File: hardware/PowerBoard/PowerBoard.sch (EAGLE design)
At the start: 134 parts, among them J1 CON-HRS-DM3AT, J2 CON-ZX62R-B-5P, J3 CON-FTSH-105-01-L-DV-K, J4 CON-S2B-PH-SM4-TB, J5 CON-PJ-102A, J6 CON-71741-0002-TOP, M1 MOUNT-HOLE3.3, M2 MOUNT-HOLE3.3, M3 MOUNT-HOLE3.3, M4 MOUNT-HOLE3.3, M5 FIDUCIAL1X2, M6 FIDUCIAL1X2, M7 FIDUCIAL1X2, M8 FIDUCIAL1X2, Q1 SI2323CDS, Q2 SI2312CDS, Q3 SI2333CDS, Q4 SI2333CDS, SW1 SWITCH-SPST, SW2 SWITCH-MS12ASG30, SW3 SWITCH-KSC-201J, U1 LTC4361-2DC, U10 MAX9938FEUK, U11 MAX9938FEUK, U12 MAX9938FEUK, U13 STM32F10XCXT6, U14 LTC2942-1, U15 USBLC6-2, U2 LTC4085, U3 XC6220B331MR-G, U4 XC6220B331MR-G, U5 XC9236A15DMR-G, U6 MIC94043, U8 MAX9938FEUK, U9 MAX9938FEUK, X1 ECX-2236, X2 ECX-31B

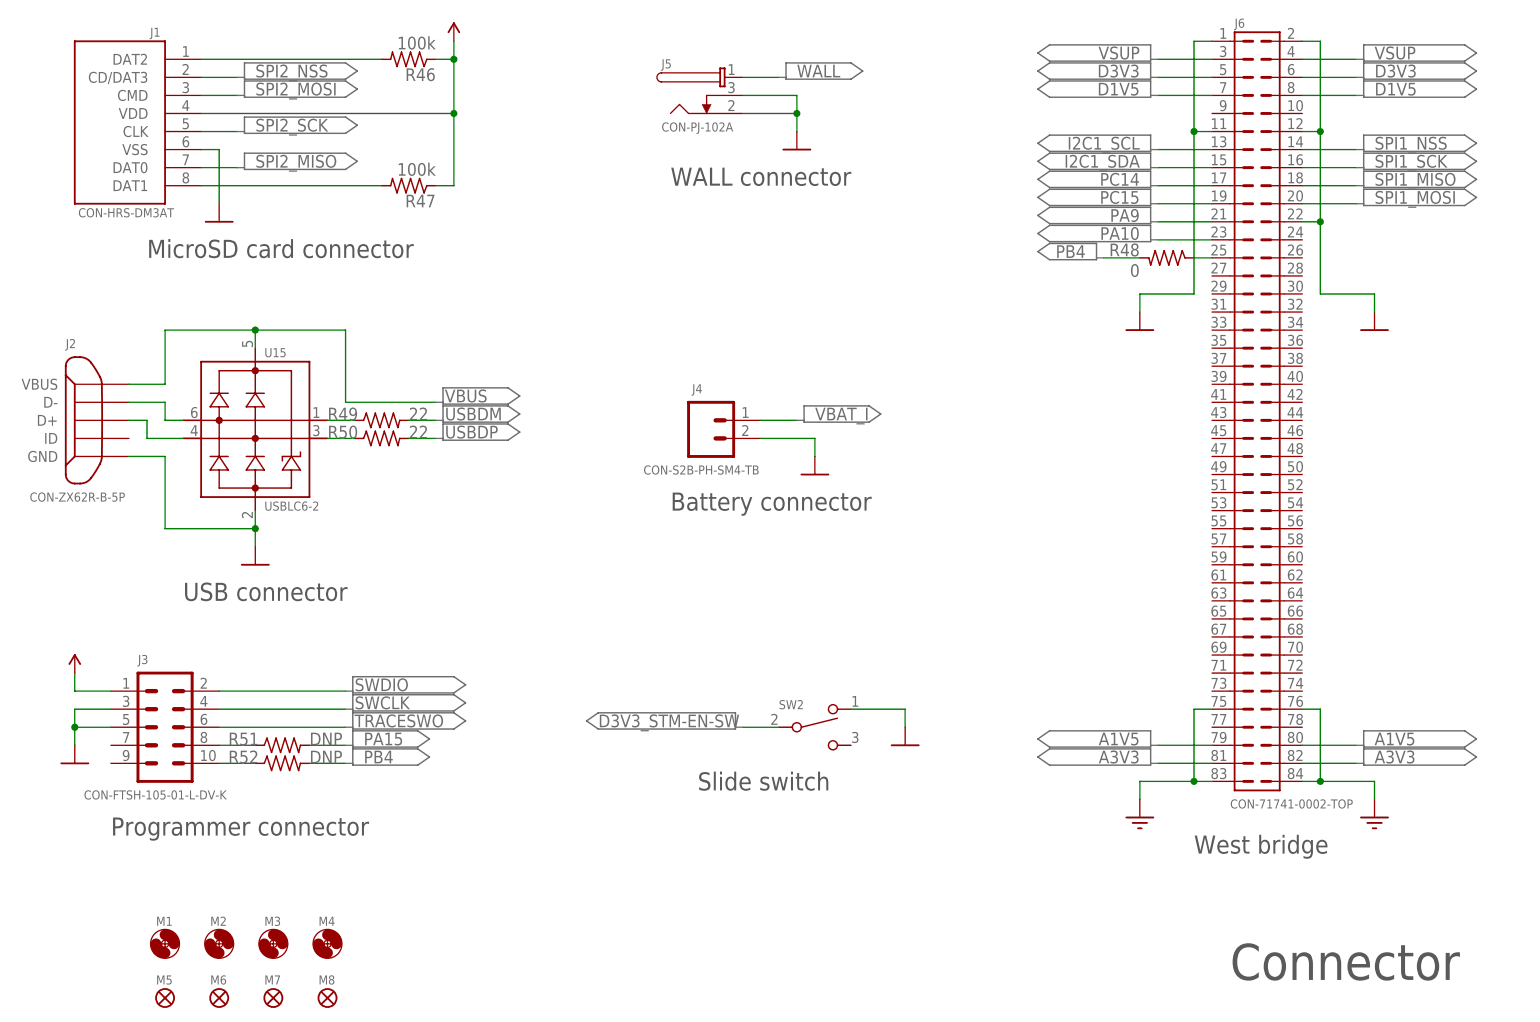
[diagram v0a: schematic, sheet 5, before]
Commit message: - Interface updated on schematic
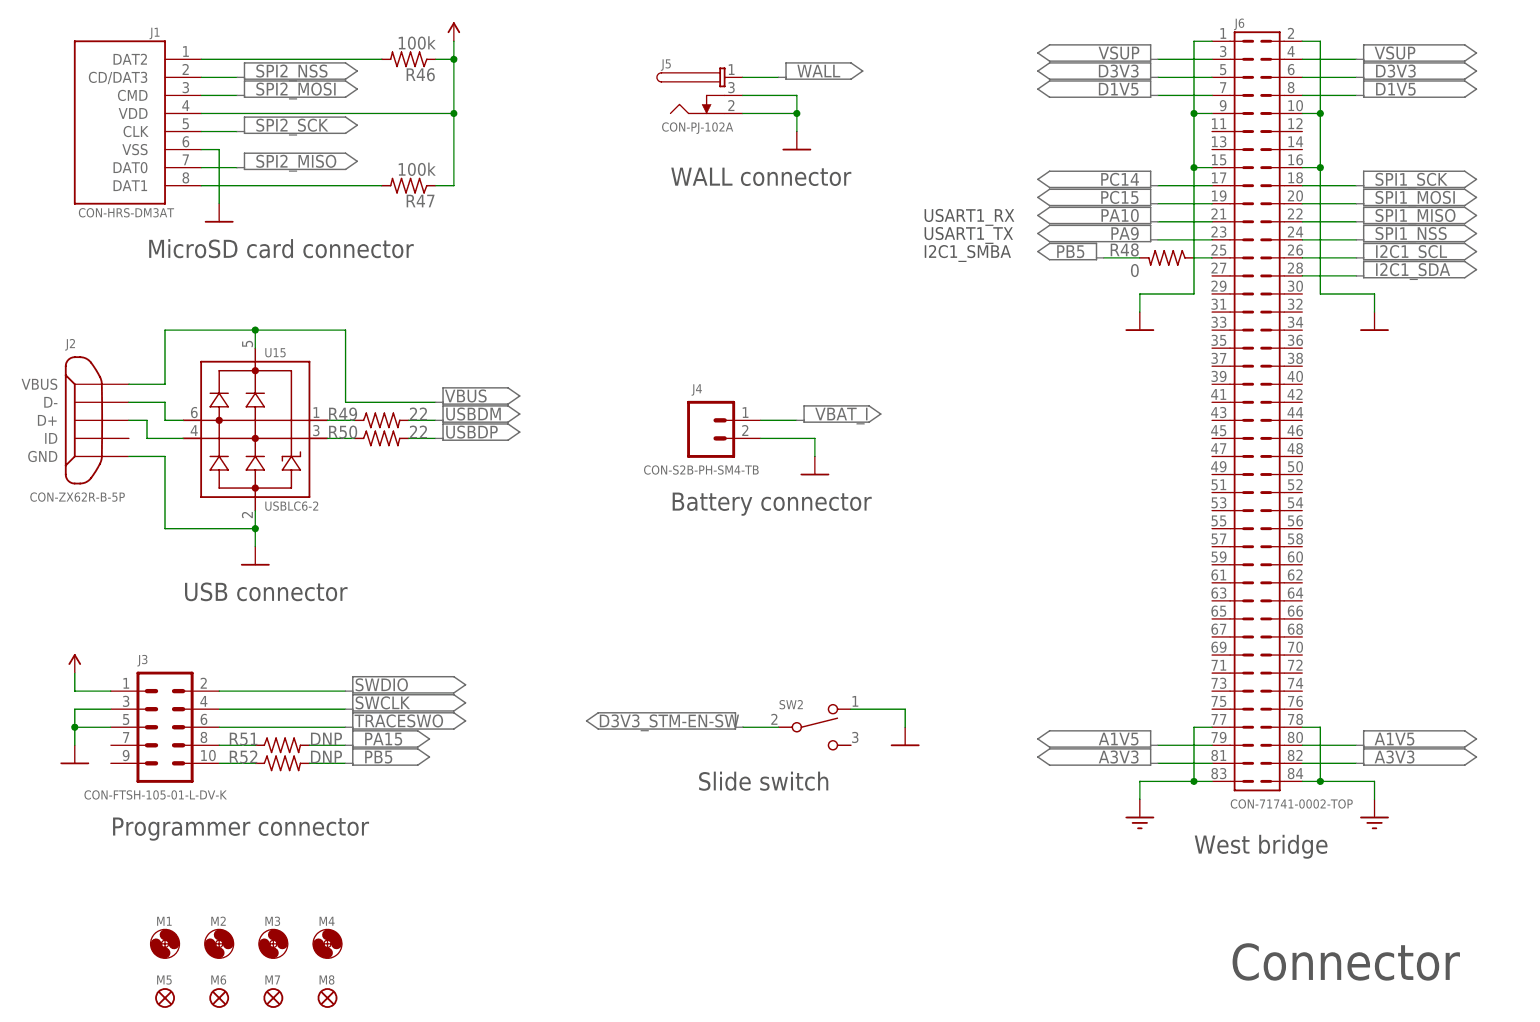
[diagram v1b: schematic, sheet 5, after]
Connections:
- net AGND: now also J6.77, J6.78; no longer J6.75, J6.76
- net DGND: now also J6.10, J6.15, J6.16, J6.9; no longer J6.11, J6.12, J6.22
- net I2C1_SCL: now also J6.26; no longer J6.13
- net I2C1_SDA: now also J6.28; no longer J6.15
- net PA10: now also J6.21; no longer J6.23
- net PA9: now also J6.23; no longer J6.21
- net PB4: now also R40.1, U14.!AL!/CC; no longer R48.2, R52.2
- net PB5: now also R48.2, R52.2; no longer R40.1, U14.!AL!/CC
- net SPI1_MISO: now also J6.22; no longer J6.18
- net SPI1_NSS: now also J6.24; no longer J6.14
- net SPI1_SCK: now also J6.18; no longer J6.16
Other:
- note added: "I2C1_SMBA"
- note added: "USART1_RX"
- note added: "USART1_TX"

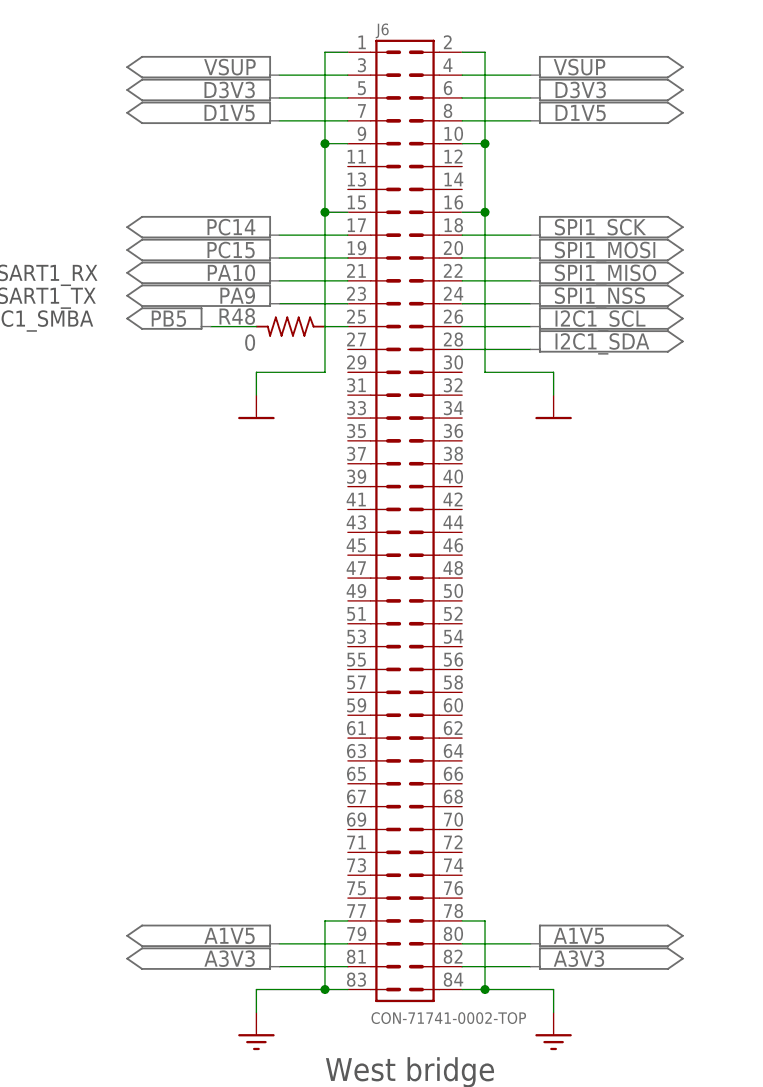
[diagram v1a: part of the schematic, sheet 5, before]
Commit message: - Components moved out of the bottom keep-out-box representing the battery - All grounds connected to mezzanine interface
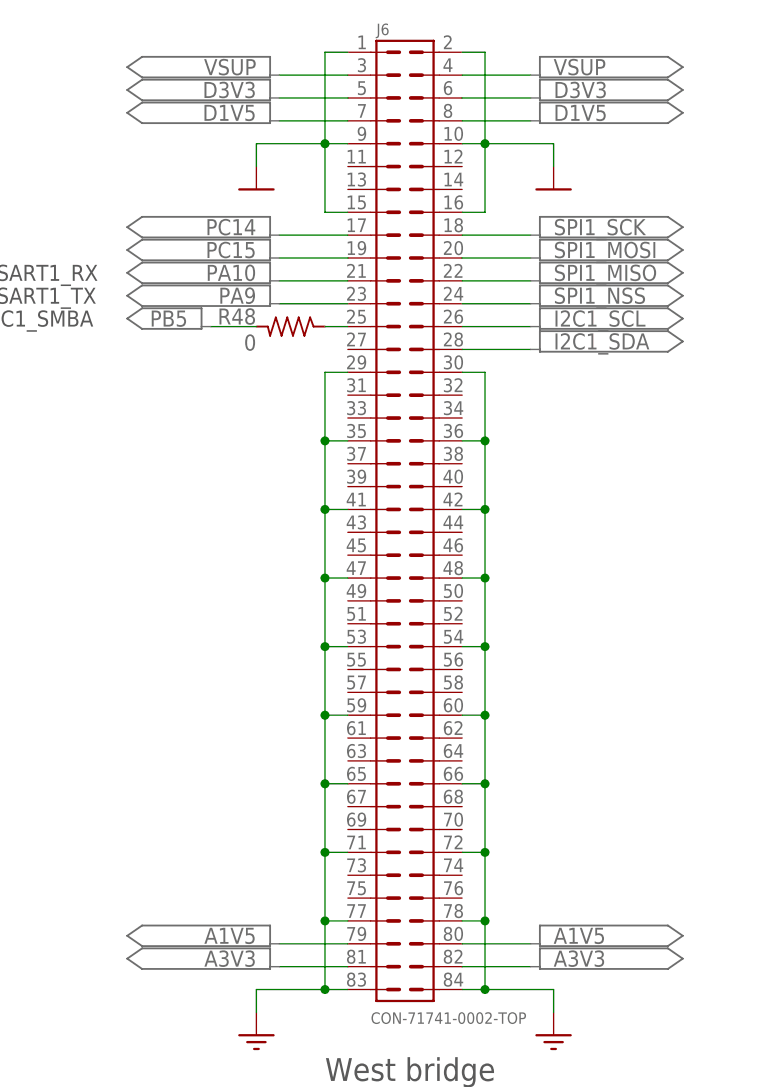
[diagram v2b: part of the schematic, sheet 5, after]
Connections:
- net AGND: now also J6.29, J6.30, J6.35, J6.36, J6.41, J6.42, J6.47, J6.48, J6.53, J6.54, J6.59, J6.60, J6.65, J6.66, J6.71, J6.72
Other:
- moved on the sheet: SW1
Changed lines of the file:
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@@
 <part name="PORT2" library="powerboard" deviceset="PORT7" device=""/>
 <part name="PORT24" library="powerboard" deviceset="PORT7" device=""/>
+<part name="PORT27" library="powerboard" deviceset="PORT15" device=""/>
 </parts>
 <sheets>
@@
 <instance part="R10" gate="G$1" x="53.34" y="86.36"/>
 <instance part="R11" gate="G$1" x="60.96" y="81.28" rot="R90"/>
-<instance part="SW1" gate="G$1" x="52.07" y="73.66"/>
-<instance part="U$63" gate="G$1" x="43.18" y="71.12"/>
+<instance part="SW1" gate="G$1" x="52.07" y="71.12"/>
+<instance part="U$63" gate="G$1" x="43.18" y="68.58"/>
 <instance part="PORT84" gate="G$1" x="203.2" y="149.86"/>
+<instance part="PORT27" gate="G$1" x="17.78" y="76.2" rot="MR0"/>
 </instances>
 <busses>
@@
 </segment>
 <segment>
-<wire x1="46.99" y1="73.66" x2="43.18" y2="73.66" width="0.1524" layer="91"/>
+<wire x1="46.99" y1="71.12" x2="43.18" y2="71.12" width="0.1524" layer="91"/>
 <pinref part="SW1" gate="G$1" pin="1"/>
 <pinref part="U$63" gate="G$1" pin="DGND"/>
@@
 <net name="D3V3_STM-EN-SW" class="0">
 <segment>
-<wire x1="57.15" y1="73.66" x2="60.96" y2="73.66" width="0.1524" layer="91"/>
-<wire x1="60.96" y1="73.66" x2="60.96" y2="76.2" width="0.1524" layer="91"/>
+<wire x1="57.15" y1="71.12" x2="60.96" y2="71.12" width="0.1524" layer="91"/>
+<wire x1="60.96" y1="71.12" x2="60.96" y2="76.2" width="0.1524" layer="91"/>
 <pinref part="SW1" gate="G$1" pin="1A"/>
 <pinref part="R11" gate="G$1" pin="1"/>
+<label x="20.32" y="76.2" size="1.778" layer="95"/>
+<wire x1="60.96" y1="76.2" x2="45.72" y2="76.2" width="0.1524" layer="91"/>
 </segment>
 </net>
@@
 <instance part="PORT87" gate="G$1" x="223.52" y="149.86"/>
 <instance part="PORT88" gate="G$1" x="223.52" y="147.32"/>
-<instance part="U$64" gate="G$1" x="210.82" y="111.76"/>
+<instance part="U$64" gate="G$1" x="210.82" y="137.16"/>
 <instance part="PORT94" gate="G$1" x="223.52" y="124.46"/>
 <instance part="PORT95" gate="G$1" x="223.52" y="132.08"/>
@@
 <instance part="PORT120" gate="G$1" x="223.52" y="50.8"/>
 <instance part="PORT89" gate="G$1" x="165.1" y="127" rot="MR0"/>
-<instance part="U$4" gate="G$1" x="177.8" y="111.76"/>
+<instance part="U$4" gate="G$1" x="177.8" y="137.16"/>
 <instance part="U15" gate="G$1" x="53.34" y="99.06"/>
 <instance part="J4" gate="G$1" x="116.84" y="96.52"/>
@@
 </segment>
 <segment>
-<wire x1="177.8" y1="114.3" x2="177.8" y2="116.84" width="0.1524" layer="91"/>
+<wire x1="177.8" y1="139.7" x2="177.8" y2="142.24" width="0.1524" layer="91"/>
 <pinref part="U$4" gate="G$1" pin="DGND"/>
 <wire x1="187.96" y1="152.4" x2="185.42" y2="152.4" width="0.1524" layer="91"/>
 <pinref part="J6" gate="G$1" pin="1"/>
 <wire x1="185.42" y1="152.4" x2="185.42" y2="142.24" width="0.1524" layer="91"/>
-<wire x1="185.42" y1="142.24" x2="185.42" y2="134.62" width="0.1524" layer="91"/>
-<wire x1="185.42" y1="134.62" x2="185.42" y2="116.84" width="0.1524" layer="91"/>
-<wire x1="177.8" y1="116.84" x2="185.42" y2="116.84" width="0.1524" layer="91"/>
+<wire x1="185.42" y1="134.62" x2="185.42" y2="142.24" width="0.1524" layer="91"/>
+<wire x1="177.8" y1="142.24" x2="185.42" y2="142.24" width="0.1524" layer="91"/>
 <pinref part="J6" gate="G$1" pin="9"/>
 <wire x1="187.96" y1="142.24" x2="185.42" y2="142.24" width="0.1524" layer="91"/>
@@
 <pinref part="J6" gate="G$1" pin="15"/>
 <wire x1="187.96" y1="134.62" x2="185.42" y2="134.62" width="0.1524" layer="91"/>
-<junction x="185.42" y="134.62"/>
-</segment>
-<segment>
-<wire x1="210.82" y1="114.3" x2="210.82" y2="116.84" width="0.1524" layer="91"/>
-<wire x1="210.82" y1="116.84" x2="203.2" y2="116.84" width="0.1524" layer="91"/>
+</segment>
+<segment>
+<wire x1="210.82" y1="139.7" x2="210.82" y2="142.24" width="0.1524" layer="91"/>
+<wire x1="210.82" y1="142.24" x2="203.2" y2="142.24" width="0.1524" layer="91"/>
 <pinref part="U$64" gate="G$1" pin="DGND"/>
 <wire x1="200.66" y1="152.4" x2="203.2" y2="152.4" width="0.1524" layer="91"/>
 <pinref part="J6" gate="G$1" pin="2"/>
-<wire x1="203.2" y1="116.84" x2="203.2" y2="134.62" width="0.1524" layer="91"/>
 <wire x1="203.2" y1="134.62" x2="203.2" y2="142.24" width="0.1524" layer="91"/>
 <wire x1="203.2" y1="142.24" x2="203.2" y2="152.4" width="0.1524" layer="91"/>
@@
 <pinref part="J6" gate="G$1" pin="16"/>
 <wire x1="200.66" y1="134.62" x2="203.2" y2="134.62" width="0.1524" layer="91"/>
-<junction x="203.2" y="134.62"/>
 </segment>
 <segment>
@@
 <wire x1="203.2" y1="55.88" x2="203.2" y2="48.26" width="0.1524" layer="91"/>
 <junction x="203.2" y="48.26"/>
+<wire x1="203.2" y1="55.88" x2="203.2" y2="63.5" width="0.1524" layer="91"/>
+<pinref part="J6" gate="G$1" pin="30"/>
+<wire x1="203.2" y1="63.5" x2="203.2" y2="71.12" width="0.1524" layer="91"/>
+<wire x1="203.2" y1="71.12" x2="203.2" y2="78.74" width="0.1524" layer="91"/>
+<wire x1="203.2" y1="78.74" x2="203.2" y2="86.36" width="0.1524" layer="91"/>
+<wire x1="203.2" y1="86.36" x2="203.2" y2="93.98" width="0.1524" layer="91"/>
+<wire x1="203.2" y1="93.98" x2="203.2" y2="101.6" width="0.1524" layer="91"/>
+<wire x1="203.2" y1="101.6" x2="203.2" y2="109.22" width="0.1524" layer="91"/>
+<wire x1="203.2" y1="109.22" x2="203.2" y2="116.84" width="0.1524" layer="91"/>
+<wire x1="203.2" y1="116.84" x2="200.66" y2="116.84" width="0.1524" layer="91"/>
+<pinref part="J6" gate="G$1" pin="72"/>
+<wire x1="203.2" y1="63.5" x2="200.66" y2="63.5" width="0.1524" layer="91"/>
+<pinref part="J6" gate="G$1" pin="66"/>
+<wire x1="203.2" y1="71.12" x2="200.66" y2="71.12" width="0.1524" layer="91"/>
+<pinref part="J6" gate="G$1" pin="60"/>
+<wire x1="203.2" y1="78.74" x2="200.66" y2="78.74" width="0.1524" layer="91"/>
+<pinref part="J6" gate="G$1" pin="54"/>
+<wire x1="203.2" y1="86.36" x2="200.66" y2="86.36" width="0.1524" layer="91"/>
+<pinref part="J6" gate="G$1" pin="48"/>
+<wire x1="203.2" y1="93.98" x2="200.66" y2="93.98" width="0.1524" layer="91"/>
+<pinref part="J6" gate="G$1" pin="42"/>
+<wire x1="203.2" y1="101.6" x2="200.66" y2="101.6" width="0.1524" layer="91"/>
+<pinref part="J6" gate="G$1" pin="36"/>
+<wire x1="203.2" y1="109.22" x2="200.66" y2="109.22" width="0.1524" layer="91"/>
+<junction x="203.2" y="55.88"/>
+<junction x="203.2" y="63.5"/>
+<junction x="203.2" y="71.12"/>
+<junction x="203.2" y="78.74"/>
+<junction x="203.2" y="86.36"/>
+<junction x="203.2" y="93.98"/>
+<junction x="203.2" y="101.6"/>
+<junction x="203.2" y="109.22"/>
 </segment>
 <segment>
@@
 <wire x1="185.42" y1="55.88" x2="185.42" y2="48.26" width="0.1524" layer="91"/>
 <junction x="185.42" y="48.26"/>
-</segment>
-</net>
+<wire x1="185.42" y1="55.88" x2="185.42" y2="63.5" width="0.1524" layer="91"/>
+<pinref part="J6" gate="G$1" pin="29"/>
+<wire x1="185.42" y1="63.5" x2="185.42" y2="71.12" width="0.1524" layer="91"/>
+<wire x1="185.42" y1="71.12" x2="185.42" y2="78.74" width="0.1524" layer="91"/>
+<wire x1="185.42" y1="78.74" x2="185.42" y2="86.36" width="0.1524" layer="91"/>
+<wire x1="185.42" y1="86.36" x2="185.42" y2="93.98" width="0.1524" layer="91"/>
+<wire x1="185.42" y1="93.98" x2="185.42" y2="101.6" width="0.1524" layer="91"/>
+<wire x1="185.42" y1="101.6" x2="185.42" y2="109.22" width="0.1524" layer="91"/>
+<wire x1="185.42" y1="109.22" x2="185.42" y2="116.84" width="0.1524" layer="91"/>
+<wire x1="185.42" y1="116.84" x2="187.96" y2="116.84" width="0.1524" layer="91"/>
+<pinref part="J6" gate="G$1" pin="35"/>
+<wire x1="187.96" y1="109.22" x2="185.42" y2="109.22" width="0.1524" layer="91"/>
+<pinref part="J6" gate="G$1" pin="41"/>
+<wire x1="187.96" y1="101.6" x2="185.42" y2="101.6" width="0.1524" layer="91"/>
+<pinref part="J6" gate="G$1" pin="47"/>
+<wire x1="187.96" y1="93.98" x2="185.42" y2="93.98" width="0.1524" layer="91"/>
+<pinref part="J6" gate="G$1" pin="53"/>
+<wire x1="187.96" y1="86.36" x2="185.42" y2="86.36" width="0.1524" layer="91"/>
+<pinref part="J6" gate="G$1" pin="59"/>
+<wire x1="187.96" y1="78.74" x2="185.42" y2="78.74" width="0.1524" layer="91"/>
+<pinref part="J6" gate="G$1" pin="65"/>
+<wire x1="187.96" y1="71.12" x2="185.42" y2="71.12" width="0.1524" layer="91"/>
+<pinref part="J6" gate="G$1" pin="71"/>
+<wire x1="187.96" y1="63.5" x2="185.42" y2="63.5" width="0.1524" layer="91"/>
+<junction x="185.42" y="109.22"/>
+<junction x="185.42" y="101.6"/>
+<junction x="185.42" y="93.98"/>
+<junction x="185.42" y="86.36"/>
+<junction x="185.42" y="78.74"/>
+<junction x="185.42" y="71.12"/>
+<junction x="185.42" y="63.5"/>
+<junction x="185.42" y="55.88"/>
+</segment>
+</net>
